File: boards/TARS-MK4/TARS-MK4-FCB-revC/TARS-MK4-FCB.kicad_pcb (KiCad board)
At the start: 2 copper layers, 86 x 79.1 mm, 70 parts, among them J101 U.FL, J102 Molex_SlimStack_2091680401_2x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, J103 Molex_SlimStack_2091680401_2x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, J104 Molex_SlimStack_Plug_2x20_P0.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, J105 Molex_SlimStack_Plug_2x20_P0.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, J106 Conn_01x03, J107 Conn_01x02, J108 Conn_01x06, J109 Conn_01x03, Q101 SSM3K16FU, SW101 FSMSM Switch, U101 MS5611-01BA03, U102 LSM6DSLTR, U103 MAX-M10S, U104 BNO086, U105 LIS3MDL, U106 KX134-1211, U107 Teensy4.1, U108 BME688, Y101 32.768kHz

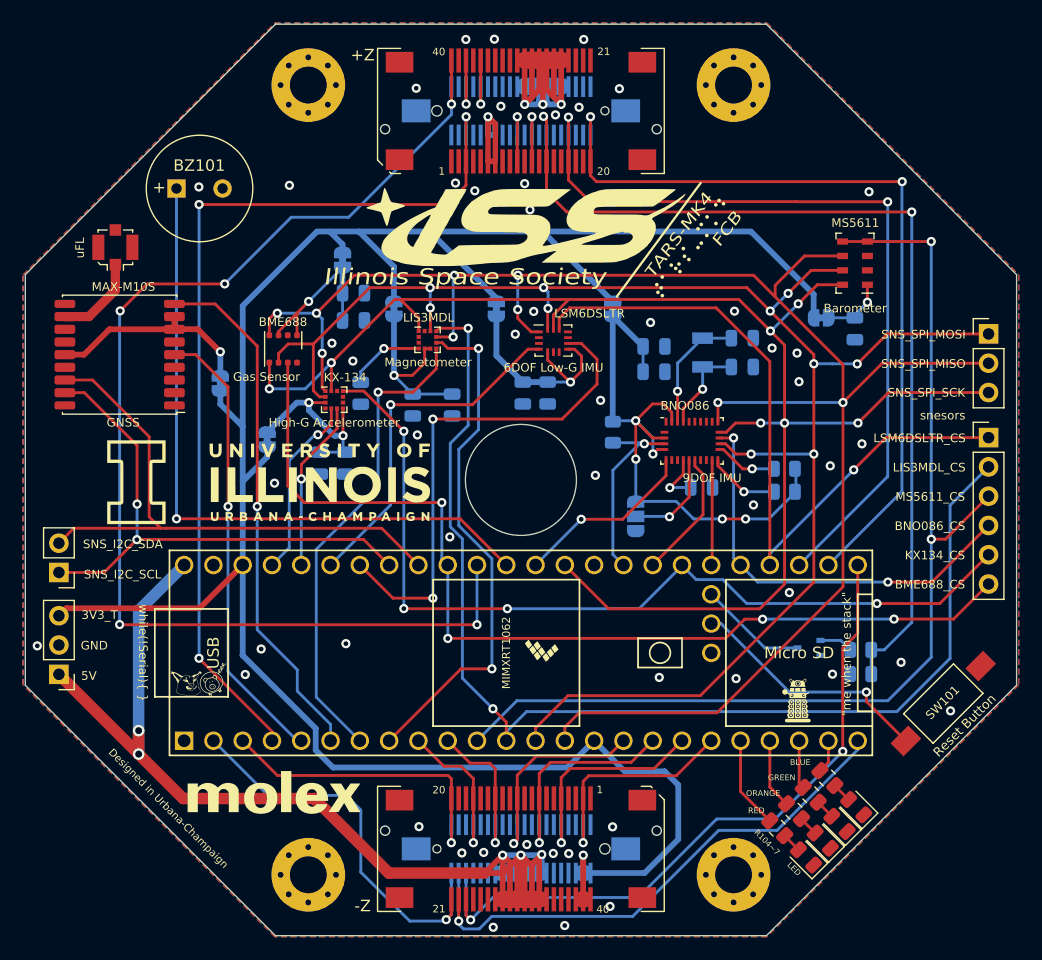
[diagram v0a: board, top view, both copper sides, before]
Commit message: Make Rev.C with mounting pin on BTB's, fixed some reference matching
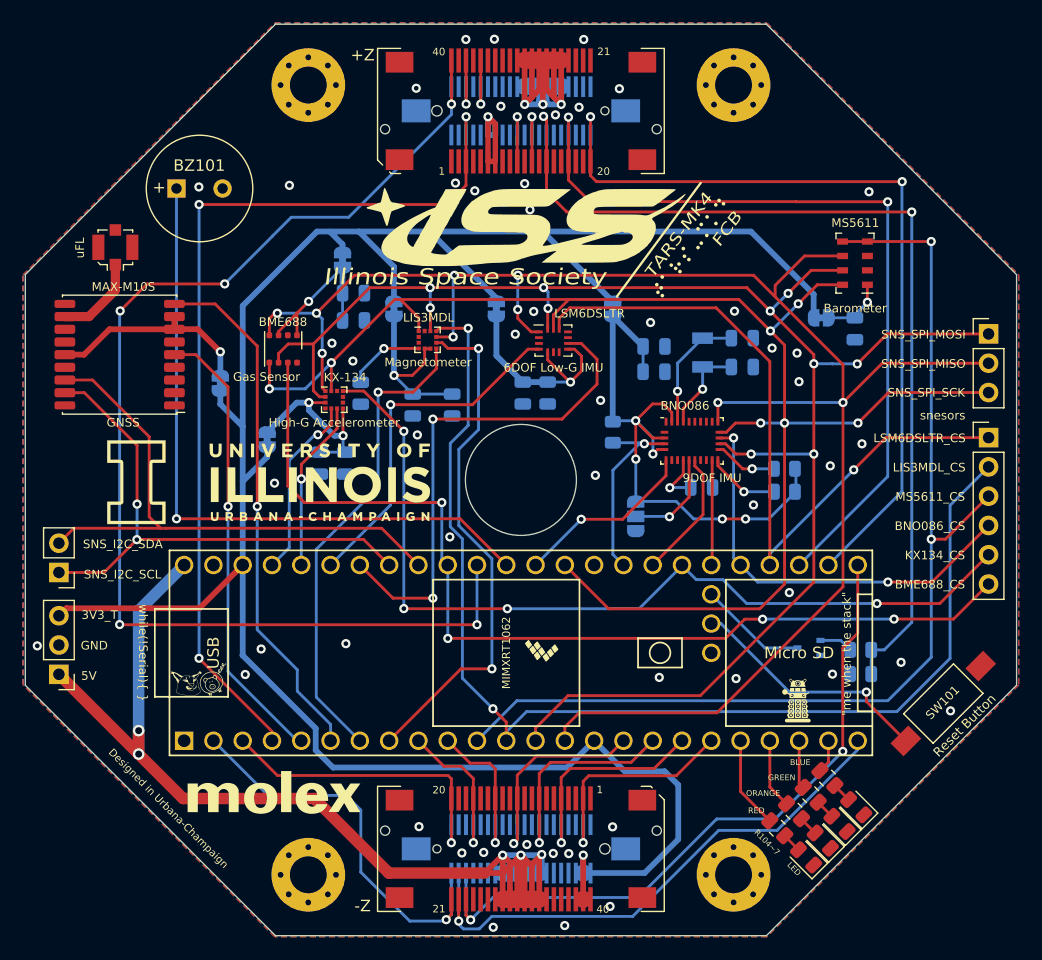
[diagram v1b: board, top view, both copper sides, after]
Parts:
- J104, J105: value Molex_SlimStack_Plug_2x20_P0.365mm -> Molex_SlimStack_Plug_550910474_2x20_P0.365mm; footprint Connector_Molex_BTB:Molex_SlimStack_Plug_536270474_2x20_P0.365mm -> Connector_Molex_BTB:Molex_SlimStack_Plug_550910474_2x20_P0.365mm
- renumbered R108 to R104, R109 to R105, R104 to R106, R105 to R107, R106 to R108, R107 to R109
